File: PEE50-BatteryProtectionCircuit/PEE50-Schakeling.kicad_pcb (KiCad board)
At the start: 2 copper layers, 108.2 x 73.7 mm, 57 parts, among them IC1 TPS7A2433DBVR, J1 Conn_01x02_Male, J2 Conn_01x02_Male, J3 Conn_01x02_Male, J4 Conn_01x02_Male, J5 Conn_02x03_Odd_Even, J6 Conn_01x02_Female, J7 Conn_01x02_Male, Q1 Q_NMOS_DGS, Q2 Q_NMOS_DGS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

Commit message: Connector voor 12V toegevoegd aan PCB en schema
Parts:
- added J8-12V: Conn_01x02_Male, Connector_Phoenix_MSTB:PhoenixContact_MSTBA_2,5_2-G-5,08_1x02_P5.08mm_Horizontal, F.Cu at (134.7, 45.6)
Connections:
- D5 pad 2: +12V -> Net-(D5-Pad2)
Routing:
- net Net-(D5-Pad2): track 0.00 -> 7.87 mm

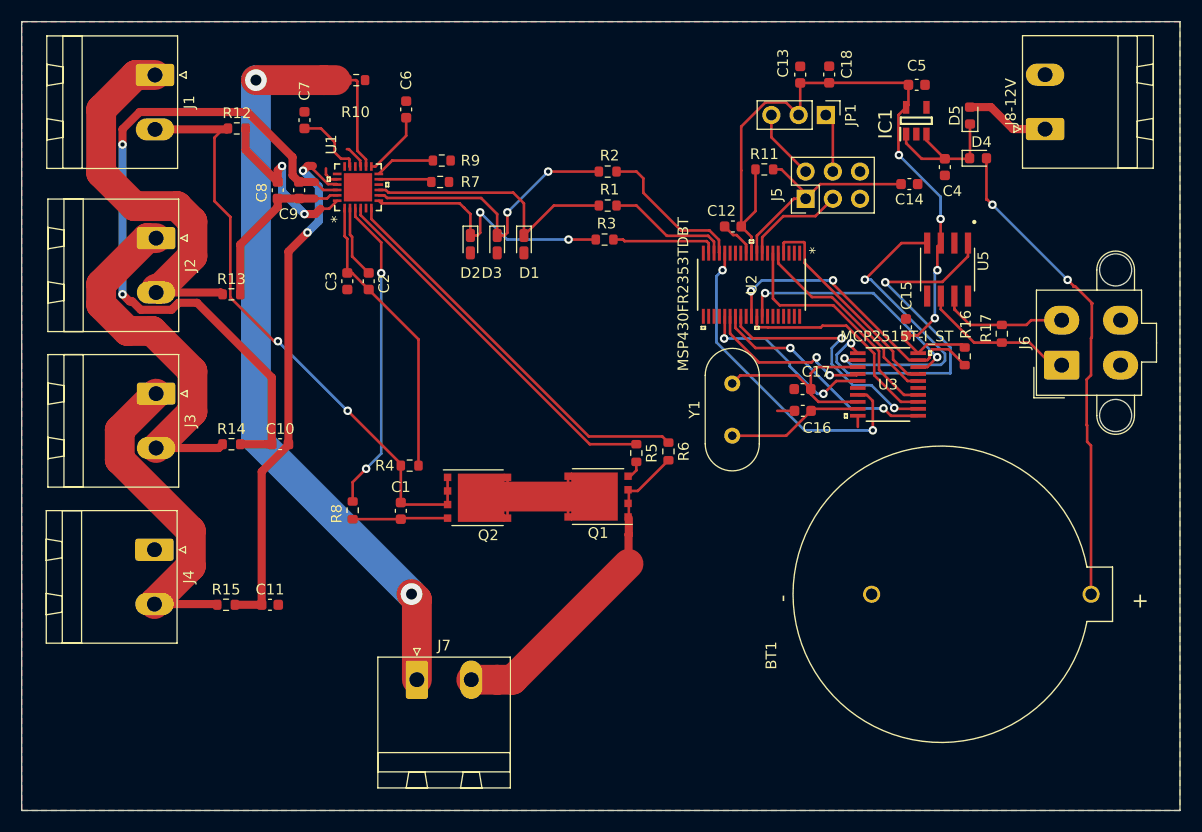
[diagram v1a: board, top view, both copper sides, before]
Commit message: 2de coincell batterij holder toegevoegd.
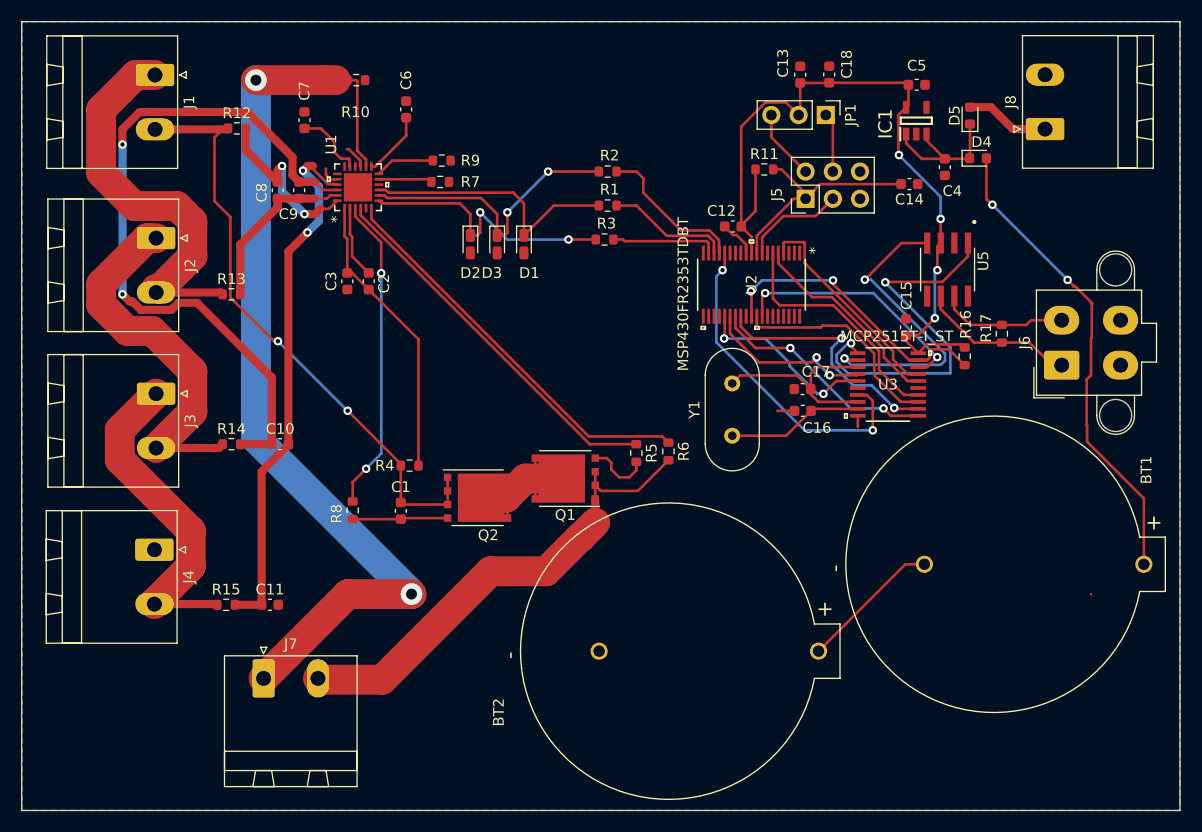
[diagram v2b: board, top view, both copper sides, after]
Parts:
- added BT2: BH1000G, CAN_control:BAT_BH1000G, F.Cu at (99.5, 94.3)
- moved J7 14.3 mm to (61.7, 96.9)
- moved BT1 5.67 mm to (129.9, 86.2)
- moved Q1 3.50 mm to (89.9, 78.2)
- renumbered J8-12V to J8
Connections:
- BT1 pad N: GND -> Net-(BT1-PadN)
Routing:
- net PositiveTerminal: track 30.9 -> 45.8 mm
- net Net-(BT1-PadN): track 0.00 -> 13.3 mm
- net NegativeTerminal: track 79.0 -> 87.9 mm
- net Net-(Q1-Pad2): track 1.76 -> 6.14 mm
- net Net-(Q1-Pad3): track 15.7 -> 14.8 mm
- net Net-(BT1-PadP): track 45.4 -> 44.6 mm

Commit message: Paar veranderingen, drill holes toegevoegd en gerber files
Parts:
- added REF**: MountingHole_2mm, MountingHole:MountingHole_2mm, F.Cu at (43.1, 106.1)
- added REF**: MountingHole_2mm, MountingHole:MountingHole_2mm, F.Cu at (93.1, 40.2)
- added REF**: MountingHole_2mm, MountingHole:MountingHole_2mm, F.Cu at (143.5, 105.9)
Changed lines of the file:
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@@
     (thickness 1.6)
     (drawings 9)
-    (tracks 524)
+    (tracks 523)
     (zones 0)
-    (modules 59)
+    (modules 62)
     (nets 86)
   )
@@
     (mod_text_size 1 1)
     (mod_text_width 0.15)
-    (pad_size 1.524 1.524)
-    (pad_drill 0.762)
+    (pad_size 10.16 10.16)
+    (pad_drill 4)
     (pad_to_mask_clearance 0)
     (aux_axis_origin 0 0)
@@
       (outputformat 1)
       (mirror false)
-      (drillshape 1)
+      (drillshape 0)
       (scaleselection 1)
       (outputdirectory ""))
@@
     (add_net PositiveTerminal)
   )
+  (module MountingHole:MountingHole_2mm (layer F.Cu)
+    (at 43.07332 106.0577)
+    (descr "Mounting Hole 2mm, no annular")
+    (tags "mounting hole 2mm no annular")
+    (attr virtual)
+    (fp_text reference REF** (at 0 -3.2) (layer F.SilkS)
+      (effects (font (size 1 1) (thickness 0.15)))
+    )
+    (fp_text value MountingHole_2mm (at 0 3.1) (layer F.Fab)
+      (effects (font (size 1 1) (thickness 0.15)))
+    )
+    (fp_text user %R (at 0.3 0) (layer F.Fab)
+      (effects (font (size 1 1) (thickness 0.15)))
+    )
+    (fp_circle (center 0 0) (end 2 0) (layer Cmts.User) (width 0.15))
+    (fp_circle (center 0 0) (end 2.25 0) (layer F.CrtYd) (width 0.05))
+    (pad "" np_thru_hole circle (at 0 0) (size 2 2) (drill 2) (layers *.Cu *.Mask))
+  )
+  (module MountingHole:MountingHole_2mm (layer F.Cu)
+    (at 93.07322 40.20058)
+    (descr "Mounting Hole 2mm, no annular")
+    (tags "mounting hole 2mm no annular")
+    (attr virtual)
+    (fp_text reference REF** (at 0 -3.2) (layer F.SilkS)
+      (effects (font (size 1 1) (thickness 0.15)))
+    )
+    (fp_text value MountingHole_2mm (at 0 3.1) (layer F.Fab)
+      (effects (font (size 1 1) (thickness 0.15)))
+    )
+    (fp_text user %R (at 0.3 0) (layer F.Fab)
+      (effects (font (size 1 1) (thickness 0.15)))
+    )
+    (fp_circle (center 0 0) (end 2 0) (layer Cmts.User) (width 0.15))
+    (fp_circle (center 0 0) (end 2.25 0) (layer F.CrtYd) (width 0.05))
+    (pad "" np_thru_hole circle (at 0 0) (size 2 2) (drill 2) (layers *.Cu *.Mask))
+  )
+  (module MountingHole:MountingHole_2mm (layer F.Cu)
+    (at 143.51 105.89514)
+    (descr "Mounting Hole 2mm, no annular")
+    (tags "mounting hole 2mm no annular")
+    (attr virtual)
+    (fp_text reference REF** (at 0 -3.2) (layer F.SilkS)
+      (effects (font (size 1 1) (thickness 0.15)))
+    )
+    (fp_text value MountingHole_2mm (at 0 3.1) (layer F.Fab)
+      (effects (font (size 1 1) (thickness 0.15)))
+    )
+    (fp_text user %R (at 0.3 0) (layer F.Fab)
+      (effects (font (size 1 1) (thickness 0.15)))
+    )
+    (fp_circle (center 0 0) (end 2 0) (layer Cmts.User) (width 0.15))
+    (fp_circle (center 0 0) (end 2.25 0) (layer F.CrtYd) (width 0.05))
+    (pad "" np_thru_hole circle (at 0 0) (size 2 2) (drill 2) (layers *.Cu *.Mask))
+  )
   (module Capacitor_SMD:C_0603_1608Metric (layer F.Cu)
     (at 74.5 81.225 270)
@@
       (effects (font (size 1 1) (thickness 0.15)))
     )
-    (fp_text user %R (at 0 0) (layer F.Fab)
-      (effects (font (size 1 1) (thickness 0.15)))
-    )
     (fp_line (start 3.4 -2.7) (end 3.4 2.7) (layer F.CrtYd) (width 0.05))
     (fp_line (start 3.4 2.7) (end -3.4 2.7) (layer F.CrtYd) (width 0.05))
@@
     (fp_line (start 3 -2.45) (end 3 2.45) (layer F.Fab) (width 0.1))
     (fp_line (start 3 2.45) (end -3 2.45) (layer F.Fab) (width 0.1))
+    (fp_text user %R (at 0 0) (layer F.Fab)
+      (effects (font (size 1 1) (thickness 0.15)))
+    )
     (pad 3 smd rect (at 2.8 0.635 180) (size 0.7 0.7) (layers F.Cu F.Paste F.Mask)
       (net 79 "Net-(Q1-Pad3)") (solder_paste_margin_ratio -0.15))
@@
   (segment (start 124.62256 58.74258) (end 124.62256 56.53024) (width 0.25) (layer F.Cu) (net 81))
   (segment (start 129.21 52.15148) (end 129.21 48.2854) (width 0.25) (layer F.Cu) (net 82))
-  (segment (start 138.98324 89.01684) (end 138.97356 89.00716) (width 0.25) (layer F.Cu) (net 82))
   (via (at 136.7917 59.64936) (size 0.8) (drill 0.4) (layers F.Cu B.Cu) (net 82))
   (via (at 129.7686 52.6288) (size 0.8) (drill 0.4) (layers F.Cu B.Cu) (net 82))
